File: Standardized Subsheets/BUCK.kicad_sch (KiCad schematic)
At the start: 11 parts, among them U6 LMR51420

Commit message: numbers
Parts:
- renumbered C17 to C15, C18 to C16, C19 to C17, C20 to C18, C21 to C19, C22 to C20, U6 to U5
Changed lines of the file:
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@@
   (symbol (lib_id "Device:C") (at 199.39 78.105 0) (unit 1)
     (in_bom yes) (on_board yes) (fields_autoplaced)
-    (property "Reference" "C22" (id 0) (at 203.2 76.8349 0)
+    (property "Reference" "C20" (id 0) (at 203.2 76.8349 0)
       (effects (font (size 1.27 1.27)) (justify left))
     )
@@
   (symbol (lib_id "power:GND") (at 193.04 81.915 0) (unit 1)
     (in_bom yes) (on_board yes) (fields_autoplaced)
-    (property "Reference" "#PWR068" (id 0) (at 193.04 88.265 0)
+    (property "Reference" "#PWR064" (id 0) (at 193.04 88.265 0)
       (effects (font (size 1.27 1.27)) hide)
     )
@@
   (symbol (lib_id "Device:C") (at 185.42 78.105 0) (unit 1)
     (in_bom yes) (on_board yes) (fields_autoplaced)
-    (property "Reference" "C21" (id 0) (at 189.23 76.8349 0)
+    (property "Reference" "C19" (id 0) (at 189.23 76.8349 0)
       (effects (font (size 1.27 1.27)) (justify left))
     )
@@
   (symbol (lib_id "Device:C") (at 92.71 83.185 0) (unit 1)
     (in_bom yes) (on_board yes) (fields_autoplaced)
-    (property "Reference" "C17" (id 0) (at 96.52 81.9149 0)
+    (property "Reference" "C15" (id 0) (at 96.52 81.9149 0)
       (effects (font (size 1.27 1.27)) (justify left))
     )
@@
   (symbol (lib_id "Device:C") (at 104.14 83.185 0) (unit 1)
     (in_bom yes) (on_board yes) (fields_autoplaced)
-    (property "Reference" "C18" (id 0) (at 107.95 81.9149 0)
+    (property "Reference" "C16" (id 0) (at 107.95 81.9149 0)
       (effects (font (size 1.27 1.27)) (justify left))
     )
@@
   (symbol (lib_id "Device:C") (at 115.57 83.185 0) (unit 1)
     (in_bom yes) (on_board yes) (fields_autoplaced)
-    (property "Reference" "C19" (id 0) (at 119.38 81.9149 0)
+    (property "Reference" "C17" (id 0) (at 119.38 81.9149 0)
       (effects (font (size 1.27 1.27)) (justify left))
     )
@@
   (symbol (lib_id "power:GND") (at 143.51 89.535 0) (unit 1)
     (in_bom yes) (on_board yes) (fields_autoplaced)
-    (property "Reference" "#PWR066" (id 0) (at 143.51 95.885 0)
+    (property "Reference" "#PWR062" (id 0) (at 143.51 95.885 0)
       (effects (font (size 1.27 1.27)) hide)
     )
@@
   (symbol (lib_id "power:GND") (at 158.75 92.075 0) (unit 1)
     (in_bom yes) (on_board yes) (fields_autoplaced)
-    (property "Reference" "#PWR067" (id 0) (at 158.75 98.425 0)
+    (property "Reference" "#PWR063" (id 0) (at 158.75 98.425 0)
       (effects (font (size 1.27 1.27)) hide)
     )
@@
   (symbol (lib_id "Regulator_Switching:TPS562200") (at 143.51 81.915 0) (unit 1)
     (in_bom yes) (on_board yes) (fields_autoplaced)
-    (property "Reference" "U6" (id 0) (at 143.51 71.755 0))
+    (property "Reference" "U5" (id 0) (at 143.51 71.755 0))
     (property "Value" "LMR51420" (id 1) (at 143.51 74.295 0))
     (property "Footprint" "Package_TO_SOT_SMD:SOT-23-6" (id 2) (at 144.78 88.265 0)
@@
   (symbol (lib_id "Device:C") (at 160.02 78.105 0) (unit 1)
     (in_bom yes) (on_board yes) (fields_autoplaced)
-    (property "Reference" "C20" (id 0) (at 163.83 76.8349 0)
+    (property "Reference" "C18" (id 0) (at 163.83 76.8349 0)
       (effects (font (size 1.27 1.27)) (justify left))
     )
@@
   (symbol (lib_id "power:PWR_FLAG") (at 96.52 78.74 0) (unit 1)
     (in_bom yes) (on_board yes) (fields_autoplaced)
-    (property "Reference" "#FLG03" (id 0) (at 96.52 76.835 0)
+    (property "Reference" "#FLG04" (id 0) (at 96.52 76.835 0)
       (effects (font (size 1.27 1.27)) hide)
     )
@@
   (symbol (lib_id "power:GND") (at 104.14 92.075 0) (unit 1)
     (in_bom yes) (on_board yes) (fields_autoplaced)
-    (property "Reference" "#PWR065" (id 0) (at 104.14 98.425 0)
-      (effects (font (size 1.27 1.27)) hide)
-    )
+    (property "Reference" "#PWR061" (id 0) (at 104.14 98.425 0)
+      (effects (font (size 1.27 1.27)) hide)
+    )

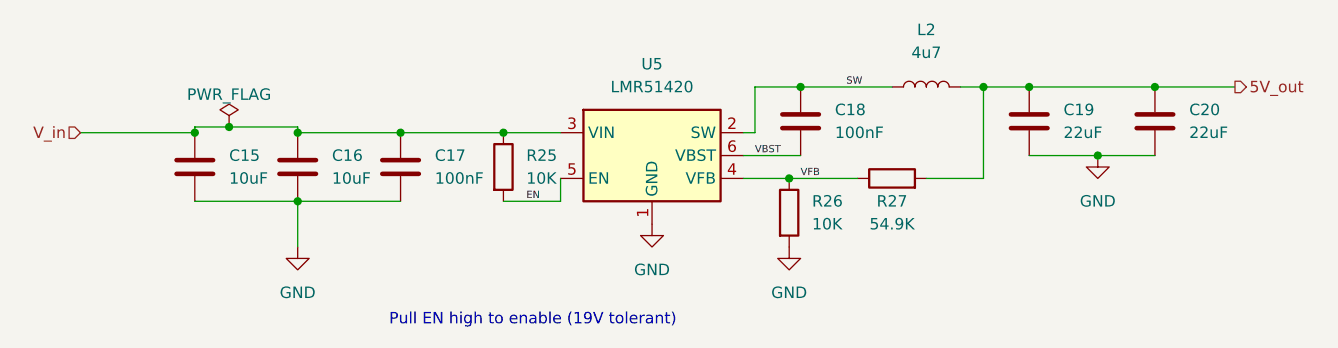
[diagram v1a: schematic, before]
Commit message: Added symbols and footprints for telemetry PCB stuffs
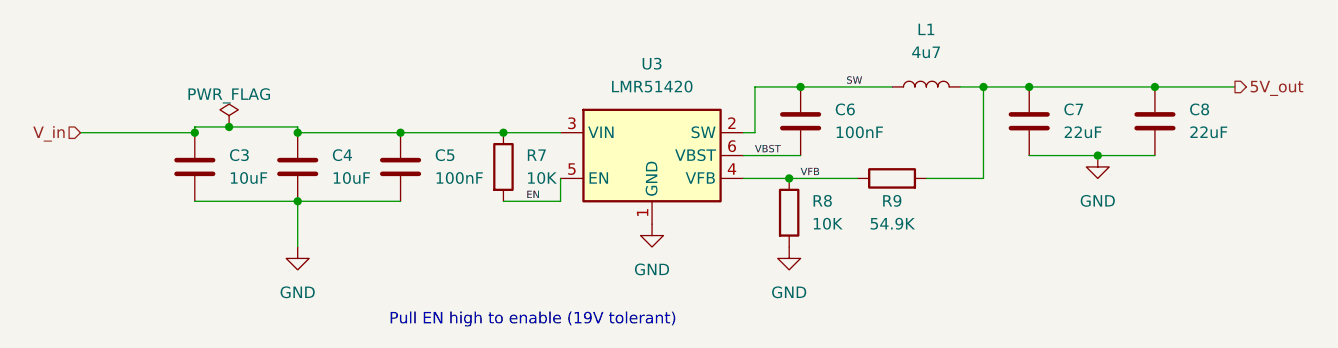
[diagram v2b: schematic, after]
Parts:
- renumbered C15 to C3, C16 to C4, C17 to C5, C18 to C6, C19 to C7, C20 to C8, L2 to L1, R25 to R7, R26 to R8, R27 to R9, U5 to U3
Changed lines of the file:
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@@
   (symbol (lib_id "Device:C") (at 199.39 78.105 0) (unit 1)
     (in_bom yes) (on_board yes) (fields_autoplaced)
-    (property "Reference" "C20" (id 0) (at 203.2 76.8349 0)
+    (property "Reference" "C8" (id 0) (at 203.2 76.8349 0)
       (effects (font (size 1.27 1.27)) (justify left))
     )
@@
   (symbol (lib_id "power:GND") (at 193.04 81.915 0) (unit 1)
     (in_bom yes) (on_board yes) (fields_autoplaced)
-    (property "Reference" "#PWR064" (id 0) (at 193.04 88.265 0)
+    (property "Reference" "#PWR041" (id 0) (at 193.04 88.265 0)
       (effects (font (size 1.27 1.27)) hide)
     )
@@
   (symbol (lib_id "Device:C") (at 185.42 78.105 0) (unit 1)
     (in_bom yes) (on_board yes) (fields_autoplaced)
-    (property "Reference" "C19" (id 0) (at 189.23 76.8349 0)
+    (property "Reference" "C7" (id 0) (at 189.23 76.8349 0)
       (effects (font (size 1.27 1.27)) (justify left))
     )
@@
   (symbol (lib_id "Device:C") (at 92.71 83.185 0) (unit 1)
     (in_bom yes) (on_board yes) (fields_autoplaced)
-    (property "Reference" "C15" (id 0) (at 96.52 81.9149 0)
+    (property "Reference" "C3" (id 0) (at 96.52 81.9149 0)
       (effects (font (size 1.27 1.27)) (justify left))
     )
@@
   (symbol (lib_id "Device:C") (at 104.14 83.185 0) (unit 1)
     (in_bom yes) (on_board yes) (fields_autoplaced)
-    (property "Reference" "C16" (id 0) (at 107.95 81.9149 0)
+    (property "Reference" "C4" (id 0) (at 107.95 81.9149 0)
       (effects (font (size 1.27 1.27)) (justify left))
     )
@@
   (symbol (lib_id "Device:C") (at 115.57 83.185 0) (unit 1)
     (in_bom yes) (on_board yes) (fields_autoplaced)
-    (property "Reference" "C17" (id 0) (at 119.38 81.9149 0)
+    (property "Reference" "C5" (id 0) (at 119.38 81.9149 0)
       (effects (font (size 1.27 1.27)) (justify left))
     )
@@
   (symbol (lib_id "power:GND") (at 143.51 89.535 0) (unit 1)
     (in_bom yes) (on_board yes) (fields_autoplaced)
-    (property "Reference" "#PWR062" (id 0) (at 143.51 95.885 0)
+    (property "Reference" "#PWR039" (id 0) (at 143.51 95.885 0)
       (effects (font (size 1.27 1.27)) hide)
     )
@@
   (symbol (lib_id "Device:R") (at 170.18 84.455 90) (unit 1)
     (in_bom yes) (on_board yes)
-    (property "Reference" "R27" (id 0) (at 170.18 86.995 90))
+    (property "Reference" "R9" (id 0) (at 170.18 86.995 90))
     (property "Value" "54.9K" (id 1) (at 170.18 89.535 90))
     (property "Footprint" "Resistor_SMD:R_0603_1608Metric_Pad0.98x0.95mm_HandSolder" (id 2) (at 170.18 86.233 90)
@@
   (symbol (lib_id "Device:R") (at 127 83.185 0) (unit 1)
     (in_bom yes) (on_board yes) (fields_autoplaced)
-    (property "Reference" "R25" (id 0) (at 129.54 81.9149 0)
+    (property "Reference" "R7" (id 0) (at 129.54 81.9149 0)
       (effects (font (size 1.27 1.27)) (justify left))
     )
@@
   (symbol (lib_id "power:GND") (at 158.75 92.075 0) (unit 1)
     (in_bom yes) (on_board yes) (fields_autoplaced)
-    (property "Reference" "#PWR063" (id 0) (at 158.75 98.425 0)
+    (property "Reference" "#PWR040" (id 0) (at 158.75 98.425 0)
       (effects (font (size 1.27 1.27)) hide)
     )
@@
   (symbol (lib_id "Regulator_Switching:TPS562200") (at 143.51 81.915 0) (unit 1)
     (in_bom yes) (on_board yes) (fields_autoplaced)
-    (property "Reference" "U5" (id 0) (at 143.51 71.755 0))
+    (property "Reference" "U3" (id 0) (at 143.51 71.755 0))
     (property "Value" "LMR51420" (id 1) (at 143.51 74.295 0))
     (property "Footprint" "Package_TO_SOT_SMD:SOT-23-6" (id 2) (at 144.78 88.265 0)
@@
   (symbol (lib_id "Device:C") (at 160.02 78.105 0) (unit 1)
     (in_bom yes) (on_board yes) (fields_autoplaced)
-    (property "Reference" "C18" (id 0) (at 163.83 76.8349 0)
+    (property "Reference" "C6" (id 0) (at 163.83 76.8349 0)
       (effects (font (size 1.27 1.27)) (justify left))
     )
@@
   (symbol (lib_id "Device:R") (at 158.75 88.265 0) (unit 1)
     (in_bom yes) (on_board yes) (fields_autoplaced)
-    (property "Reference" "R26" (id 0) (at 161.29 86.9949 0)
+    (property "Reference" "R8" (id 0) (at 161.29 86.9949 0)
       (effects (font (size 1.27 1.27)) (justify left))
     )
@@
   (symbol (lib_id "power:PWR_FLAG") (at 96.52 78.74 0) (unit 1)
     (in_bom yes) (on_board yes) (fields_autoplaced)
-    (property "Reference" "#FLG04" (id 0) (at 96.52 76.835 0)
+    (property "Reference" "#FLG05" (id 0) (at 96.52 76.835 0)
       (effects (font (size 1.27 1.27)) hide)
     )
@@
   (symbol (lib_id "Device:L") (at 173.99 74.295 90) (unit 1)
     (in_bom yes) (on_board yes) (fields_autoplaced)
-    (property "Reference" "L2" (id 0) (at 173.99 67.945 90))
+    (property "Reference" "L1" (id 0) (at 173.99 67.945 90))
     (property "Value" "4u7" (id 1) (at 173.99 70.485 90))
     (property "Footprint" "Inductor_SMD:L_Sunlord_MWSA0518_5.4x5.2mm" (id 2) (at 173.99 74.295 0)
       (effects (font (size 1.27 1.27)) hide)
     )
-    (property "Datasheet" "https://datasheet.lcsc.com/lcsc/1912111437_Sunlord-MWSA0503S-4R7MT_C408410.pdf" (id 3) (at 173.99 74.295 0)
+    (property "Datasheet" "~" (id 3) (at 173.99 74.295 0)
       (effects (font (size 1.27 1.27)) hide)
     )
@@
   (symbol (lib_id "power:GND") (at 104.14 92.075 0) (unit 1)
     (in_bom yes) (on_board yes) (fields_autoplaced)
-    (property "Reference" "#PWR061" (id 0) (at 104.14 98.425 0)
-      (effects (font (size 1.27 1.27)) hide)
-    )
+    (property "Reference" "#PWR038" (id 0) (at 104.14 98.425 0)
+      (effects (font (size 1.27 1.27)) hide)
+    )
